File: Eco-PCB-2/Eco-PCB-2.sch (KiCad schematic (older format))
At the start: 15 parts, among them J1 DB25_Female, J2 Switch, P1 Push Button, P2 Push Button

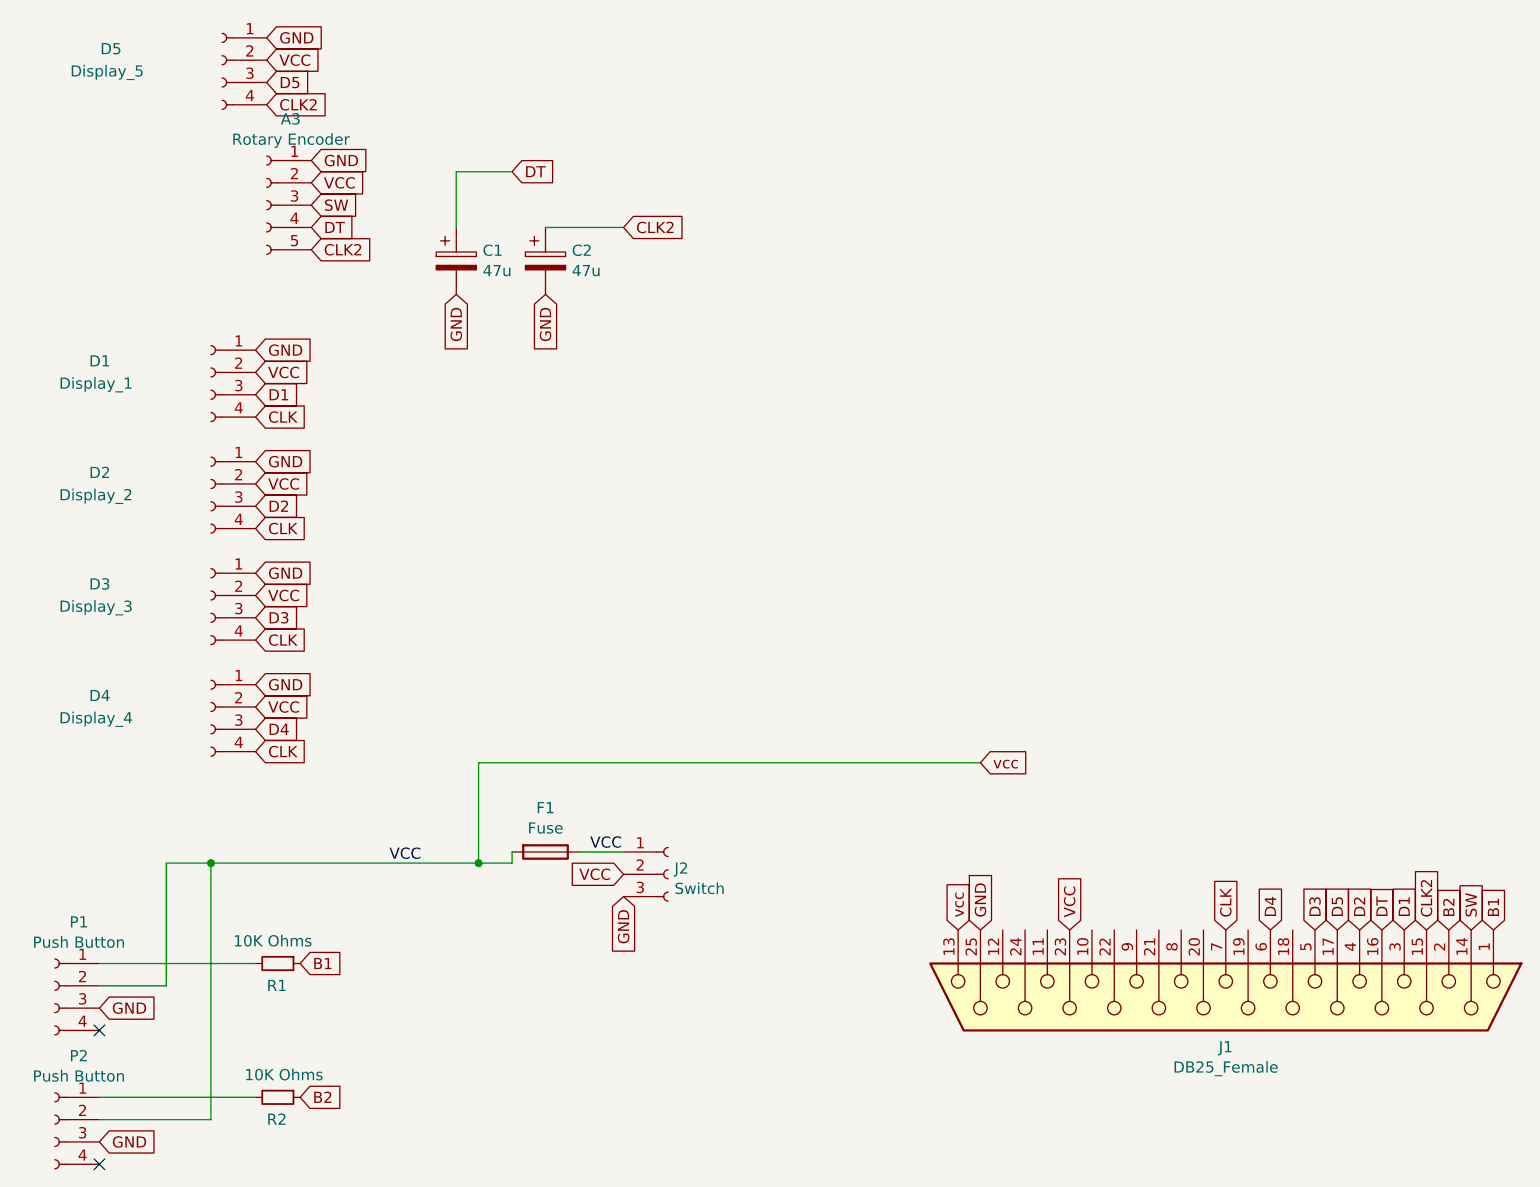
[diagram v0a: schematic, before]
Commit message: updated pin sizes issue and spacing on PCB2
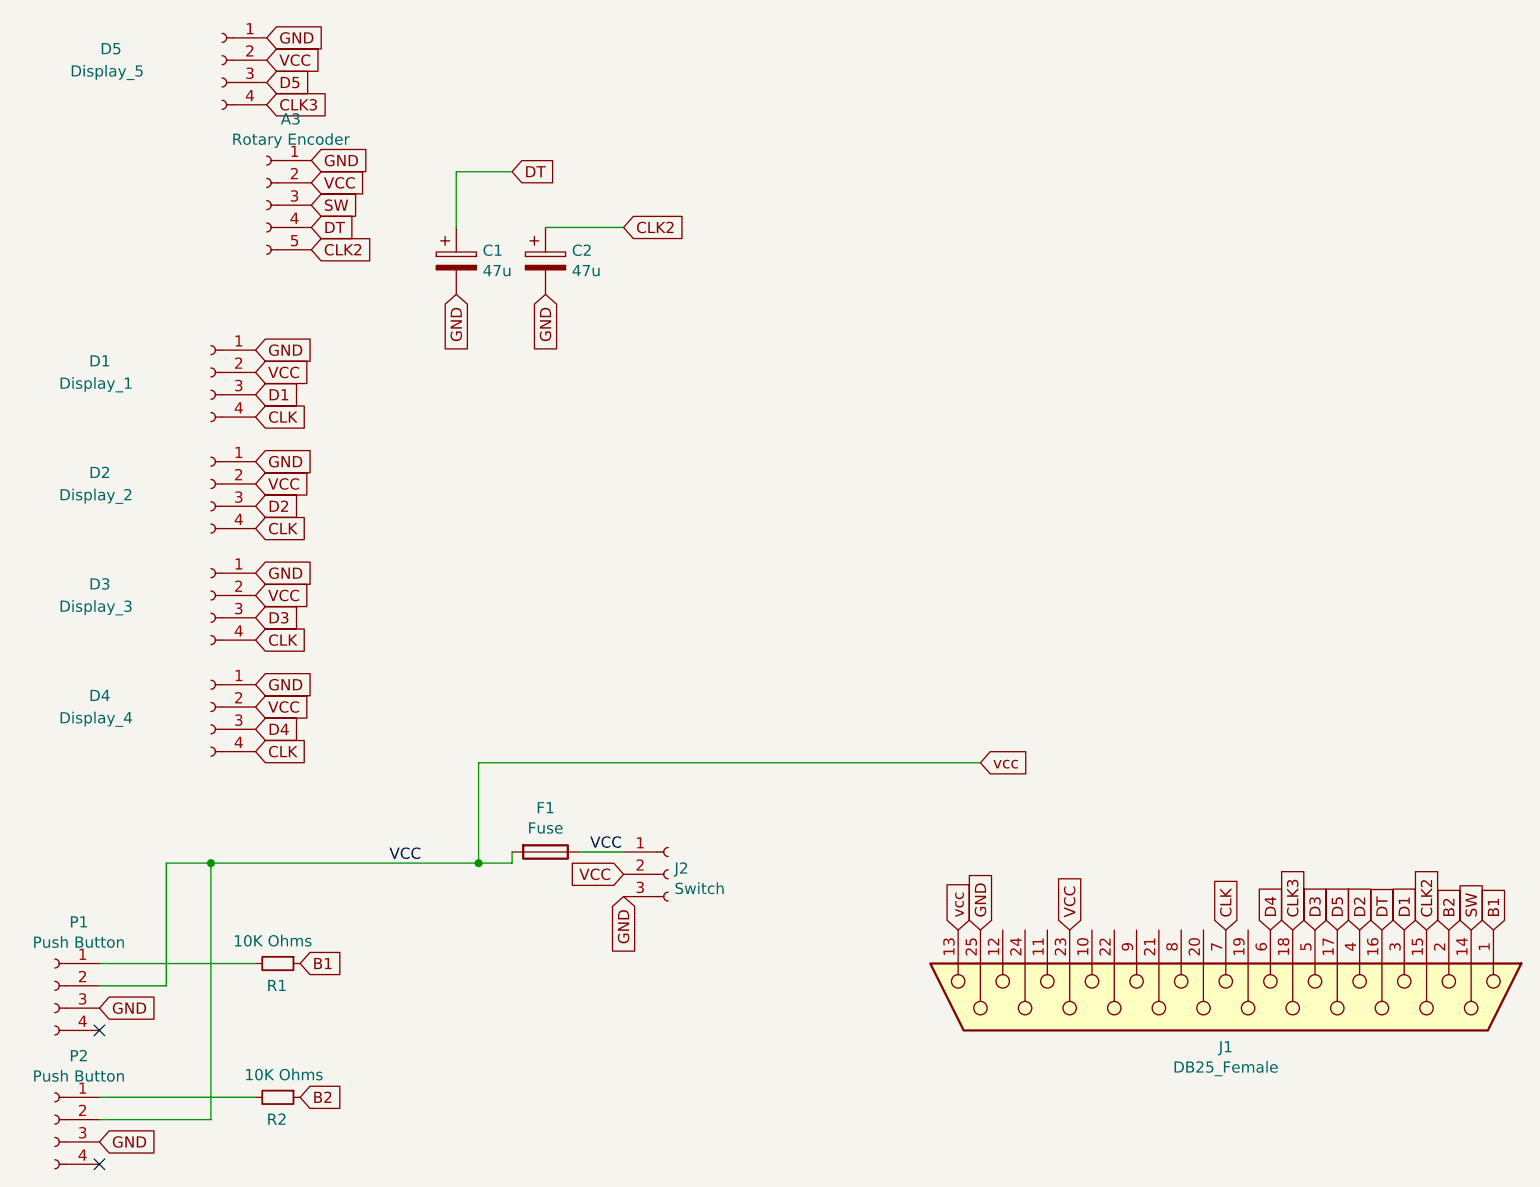
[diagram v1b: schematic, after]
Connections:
- net CLK2: no longer D5.4 (Pin_4)
- net CLK3: now reaches J1.18 (P18)
- net CLK3: now also D5.4 (Pin_4)
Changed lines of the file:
@@
 CLK2
 Text GLabel 5200 2200 2    50   Input ~ 0
-CLK2
+CLK3
 Text GLabel 8800 5900 1    50   Input ~ 0
 VCC
@@
 Text GLabel 4450 6250 2    50   Input ~ 0
 GND
+Text GLabel 9800 5900 1    50   Input ~ 0
+CLK3
 $EndSCHEMATC
